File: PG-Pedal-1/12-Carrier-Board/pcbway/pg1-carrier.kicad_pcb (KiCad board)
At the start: 2 copper layers, 111 x 42.2 mm, 97 parts, among them J1 line in, J10 seed audio, J19 pg-hp, J2 line out, J20 pg-line, J3 no amp, J4 phones, J9 9V in, U1 LP2985-33, U4 NE5532, U5 NE5532, U6 NE5532, U7 TPA6139A2, U8 TPA6139A2, U9 TLV7031

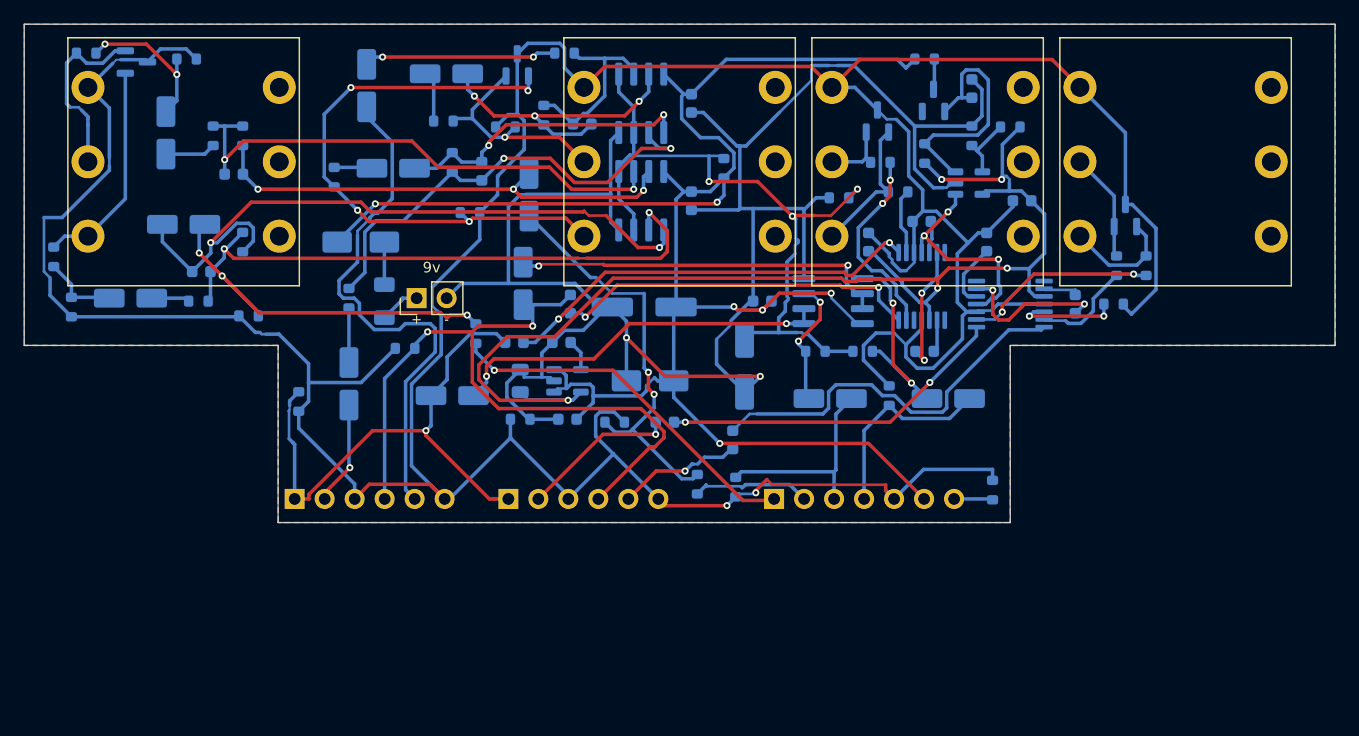
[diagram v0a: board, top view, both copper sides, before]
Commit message: Carrier board: JLCPCB files (basic parts where possible), ceramic caps instead of electrolytics
Co-Authored-By: Claude Opus 5.5 <noreply@anthropic.com>
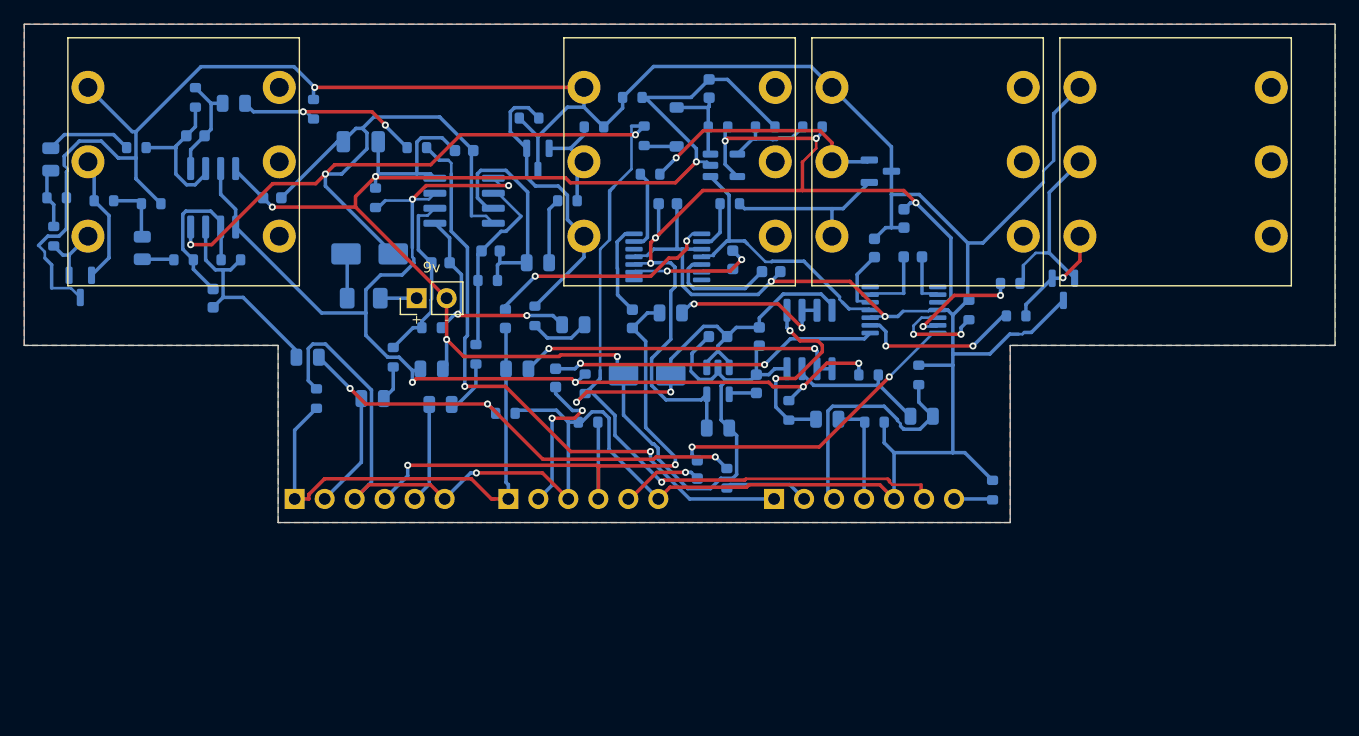
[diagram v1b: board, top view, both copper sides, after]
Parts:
- C1: value 47uF 25V -> 22uF 25V; footprint CP_Elec_6.3x5.8 -> C_1206_3216Metric
- C10, C12, C13, C14, C15, C17, C30, C32, C33, C34, C35, C37: footprint CP_Elec_4x5.4 -> C_0805_2012Metric
- C2: value 47uF 16V -> 22uF 25V; footprint CP_Elec_5x5.4 -> C_0805_2012Metric
- D50: value BAT54 -> 1N4148W; footprint SOT-23 -> D_SOD-123
- R18, R38: value 22k -> 51k
- R19, R39: value 43k -> 100k
- moved R2 39.2 mm to (74.2, 44.5), turned to 90 degrees
- moved U4 36.3 mm to (60.5, 44.5), turned to -90 degrees
- moved C66 35.5 mm to (65.5, 44.5), turned to 180 degrees
- moved R70 28.9 mm to (96.0, 36.0)
- moved C1 27.8 mm to (73.0, 39.8), turned to 0 degrees
- moved C35 27.7 mm to (79.8, 62.0), turned to 180 degrees
- moved R38 26.6 mm to (82.8, 57.8), turned to 90 degrees
- moved C2 26.5 mm to (79.0, 59.0), turned to 0 degrees
- moved R51 24.6 mm to (97.0, 39.2), turned to -90 degrees
- moved C32 23.3 mm to (68.5, 58.0), turned to 0 degrees
- moved C50 22.2 mm to (102.5, 35.2)
- moved D50 21.9 mm to (99.8, 38.5)
- moved R1 21.7 mm to (92.0, 60.2)
- moved U7 21.6 mm to (99.0, 49.5), turned to 180 degrees
- moved U9 20.8 mm to (103.8, 41.8)
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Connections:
- D50 pad 1: EN_RC -> +9V_SENSE
- D50 pad 2: (no net) -> EN_RC
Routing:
- net IN_O_L: track 57.7 -> 9.09 mm, vias 2 -> 0
- net IN_N_L: track 50.7 -> 12.6 mm, vias 2 -> 0
- net VREF: track 61.8 -> 99.3 mm, vias 3 -> 6
- net LINE_W_R: track 44.9 -> 8.51 mm
- net IN_N_R: track 45.1 -> 14.4 mm, vias 2 -> 0
- net +9V: track 154.8 -> 182.1 mm
- net JLO_L: track 50.2 -> 24.8 mm, vias 4 -> 0
- net LO_N_L: track 39.2 -> 15.1 mm, vias 2 -> 0
- net NA_IN_R: track 30.9 -> 7.99 mm, vias 2 -> 0
- net IN_O_R: track 41.1 -> 18.6 mm, vias 3 -> 0
- net +3V3A: track 104.8 -> 82.6 mm
- net SEED_IN_L: track 31.2 -> 52.7 mm, vias 1 -> 2
- net OB_O_R: track 32.3 -> 14.1 mm
- net SEED_IN_RAW_L: track 33.5 -> 16.4 mm, vias 3 -> 2
- net NA_IN_L: track 35.9 -> 19.9 mm
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
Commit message: Carrier board: all parts on one side, labels clear of pads, 0 DRC warnings
Co-Authored-By: Claude Opus 5.5 <noreply@anthropic.com>
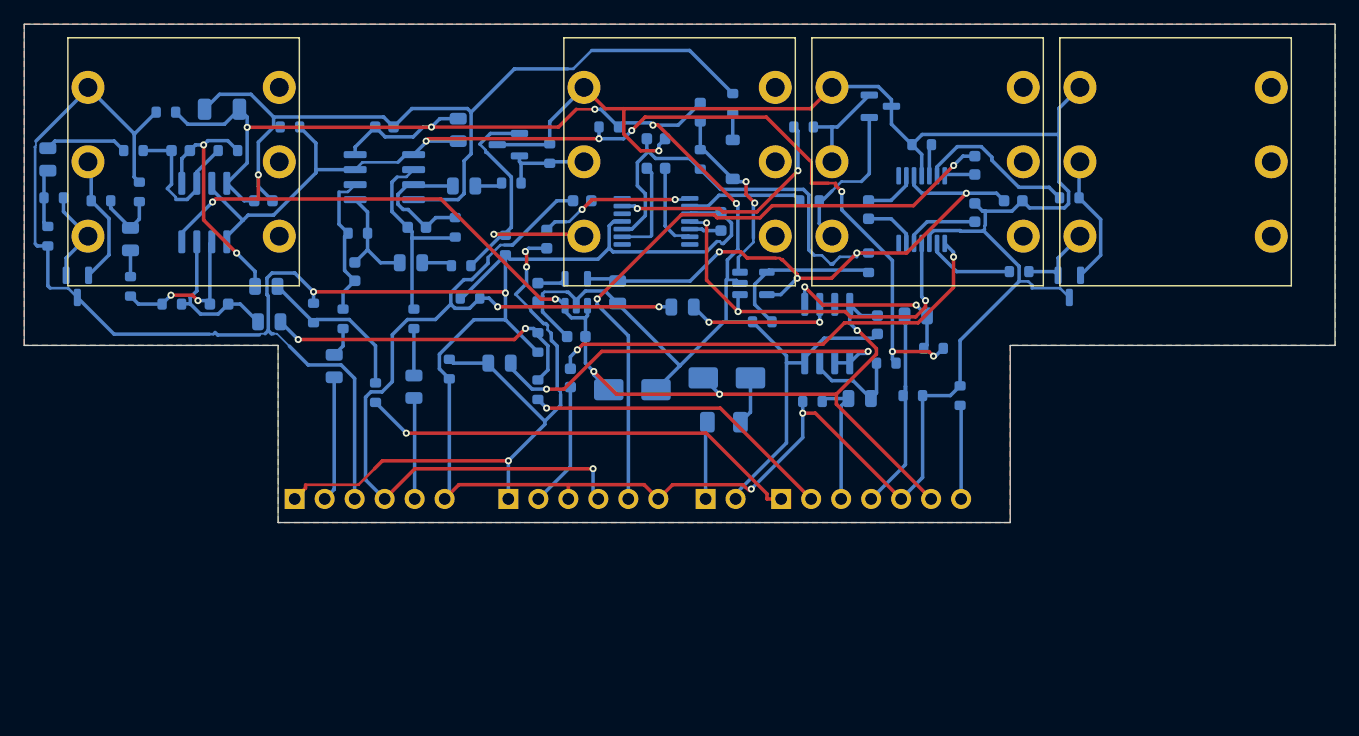
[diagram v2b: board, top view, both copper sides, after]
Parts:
- J9: footprint PinHeader_1x02_P2.54mm_Vertical -> PinHeader_1x02_P2.54mm_Horizontal; moved to B.Cu
- moved R70 39.5 mm to (56.5, 37.2)
- moved C39 34.9 mm to (125.0, 41.8), turned to -90 degrees
- moved R1 33.1 mm to (67.0, 38.5), turned to 0 degrees
- moved F1 32.3 mm to (103.8, 63.5), turned to 0 degrees
- moved D1 32.0 mm to (104.0, 59.8), turned to 0 degrees
- moved J9 29.8 mm to (102.2, 70.0), turned to -90 degrees
- moved R13 21.0 mm to (74.2, 61.0), turned to -90 degrees
- moved R2 20.6 mm to (94.0, 38.5), turned to 0 degrees
- moved C2 20.4 mm to (81.2, 38.8), turned to 90 degrees
- moved C3 20.1 mm to (88.0, 52.5), turned to -90 degrees
- moved R33 17.7 mm to (88.0, 60.8)
- moved R14 17.2 mm to (69.0, 54.2)
- moved R53 16.5 mm to (107.0, 55.0), turned to 180 degrees
- moved C12 15.7 mm to (65.0, 52.0)
- moved C17 14.7 mm to (77.2, 50.0)
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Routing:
- net HP_W_R: track 6.99 -> 55.2 mm, vias 1 -> 2
- net BUS_R: track 51.6 -> 77.9 mm, vias 2 -> 3
- net HP_IN_R: track 26.1 -> 2.60 mm, vias 2 -> 0
- net SEED_IN_R: track 7.17 -> 26.6 mm, vias 0 -> 1
- net SEED_IN_L: track 52.7 -> 38.0 mm, vias 2 -> 1
- net BUS_L: track 42.8 -> 56.8 mm, vias 0 -> 3
- net NA_O_R: track 6.88 -> 20.4 mm, vias 0 -> 2
- net JNA_R: track 21.4 -> 8.81 mm, vias 1 -> 0
- net IN_O_L: track 9.09 -> 21.6 mm, vias 0 -> 2
- net +9V: track 182.1 -> 170.0 mm
- net SEED_IN_RAW_R: track 39.7 -> 27.7 mm, vias 3 -> 2
- net HP_IN_L: track 28.0 -> 39.9 mm
- net LO_O_L: track 19.8 -> 9.38 mm, vias 2 -> 0
- net SEED_OUT_L: track 21.3 -> 11.1 mm
- net MUTE_N: track 23.6 -> 33.5 mm, vias 0 -> 3
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
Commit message: Carrier board: Neutrik NMJ6HCD2 jacks fitted by the assembler; jack holes 11.4 mm
Co-Authored-By: Claude Opus 5.5 <noreply@anthropic.com>
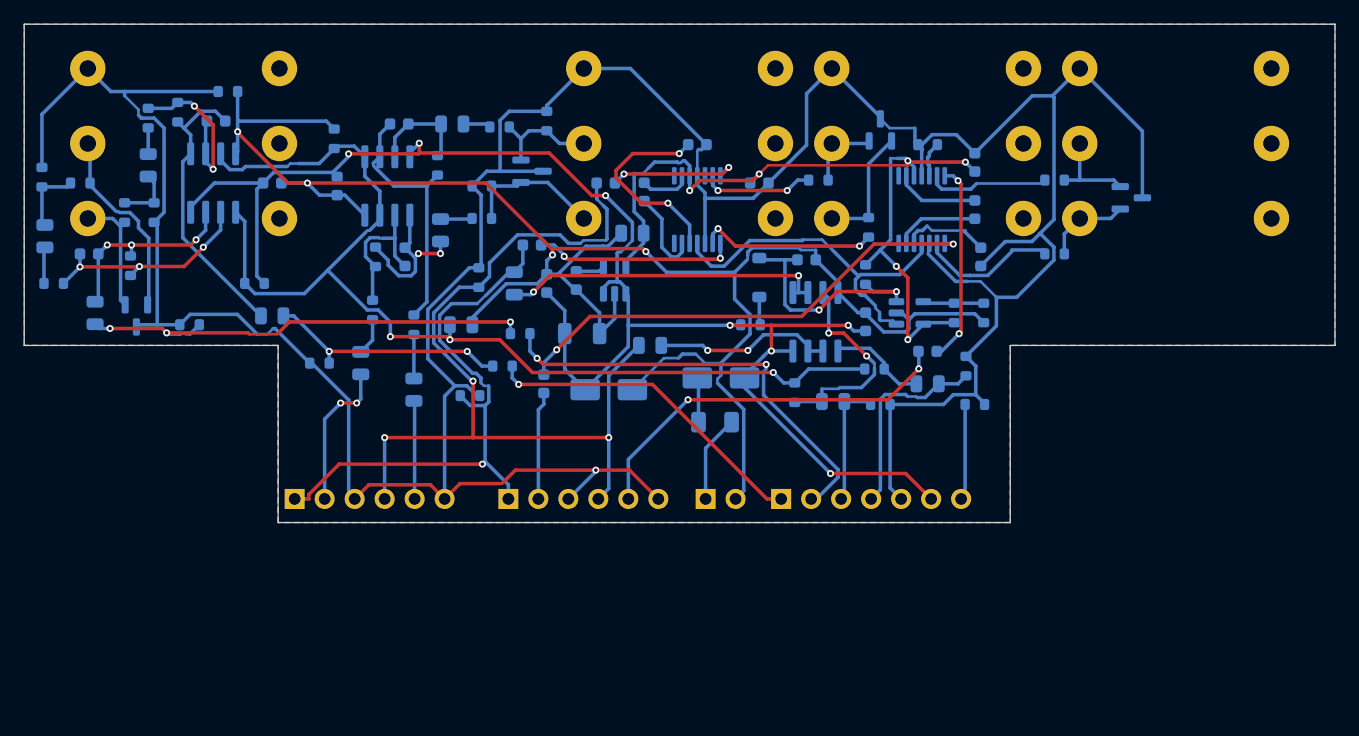
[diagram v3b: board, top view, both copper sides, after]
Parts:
- J1, J2, J3, J4: footprint Jack_6.35mm_TRS_PCB_A-1122 -> Jack_6.35mm_Neutrik_NMJ6HCD2_Horizontal
- moved C1 35.9 mm to (91.8, 56.0)
- moved R34 29.5 mm to (58.5, 55.2), turned to 180 degrees
- moved R2 23.3 mm to (70.8, 39.5), turned to 90 degrees
- moved R51 18.8 mm to (106.0, 55.2), turned to 0 degrees
- moved R53 18.8 mm to (125.8, 54.2), turned to -90 degrees
- moved J4 17.3 mm to (133.9, 46.2), turned to 90 degrees
- moved J1 17.3 mm to (49.9, 46.2), turned to 90 degrees
- moved J2 17.3 mm to (91.9, 46.2), turned to 90 degrees
- moved J3 17.3 mm to (112.9, 46.2), turned to 90 degrees
- moved R50 17.1 mm to (115.8, 51.0), turned to -90 degrees
- moved C2 16.5 mm to (81.5, 55.2), turned to 0 degrees
- moved C39 16.2 mm to (121.0, 57.5), turned to 0 degrees
- moved C50 15.4 mm to (110.8, 49.8), turned to 0 degrees
- moved C32 14.8 mm to (50.5, 54.2), turned to -90 degrees
- moved R1 13.6 mm to (64.0, 51.8), turned to 180 degrees
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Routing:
- net +9V: track 170.0 -> 131.6 mm, vias 6 -> 7
- net AGND: track 338.3 -> 306.3 mm, vias 5 -> 1
- net HP_W_R: track 55.2 -> 32.6 mm
- net +3V3A: track 85.0 -> 69.2 mm, vias 4 -> 6
- net NA_VSS: track 2.69 -> 17.1 mm, vias 0 -> 2
- net HP_IN_R: track 2.60 -> 16.9 mm, vias 0 -> 2
- net JLO_L: track 25.5 -> 11.9 mm, vias 1 -> 0
- net SEED_IN_RAW_R: track 27.7 -> 40.2 mm, vias 2 -> 3
- net NA_O_R: track 20.4 -> 9.48 mm
- net SEED_IN_R: track 26.6 -> 37.3 mm, vias 1 -> 2
- net GND: track 147.8 -> 158.2 mm, vias 5 -> 4
- net SEED_IN_L: track 38.0 -> 28.0 mm
- net EN_REF: track 14.0 -> 5.16 mm
- net OB_P_L: track 9.06 -> 17.9 mm, vias 0 -> 2
- net OB_O_L: track 36.1 -> 27.4 mm
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
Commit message: Carrier board: inputs left / outputs right with a diamond divider, (IN)/(OUT) labels, pg-1 artwork; face print IN/OUT tags
Co-Authored-By: Claude Opus 5.5 <noreply@anthropic.com>
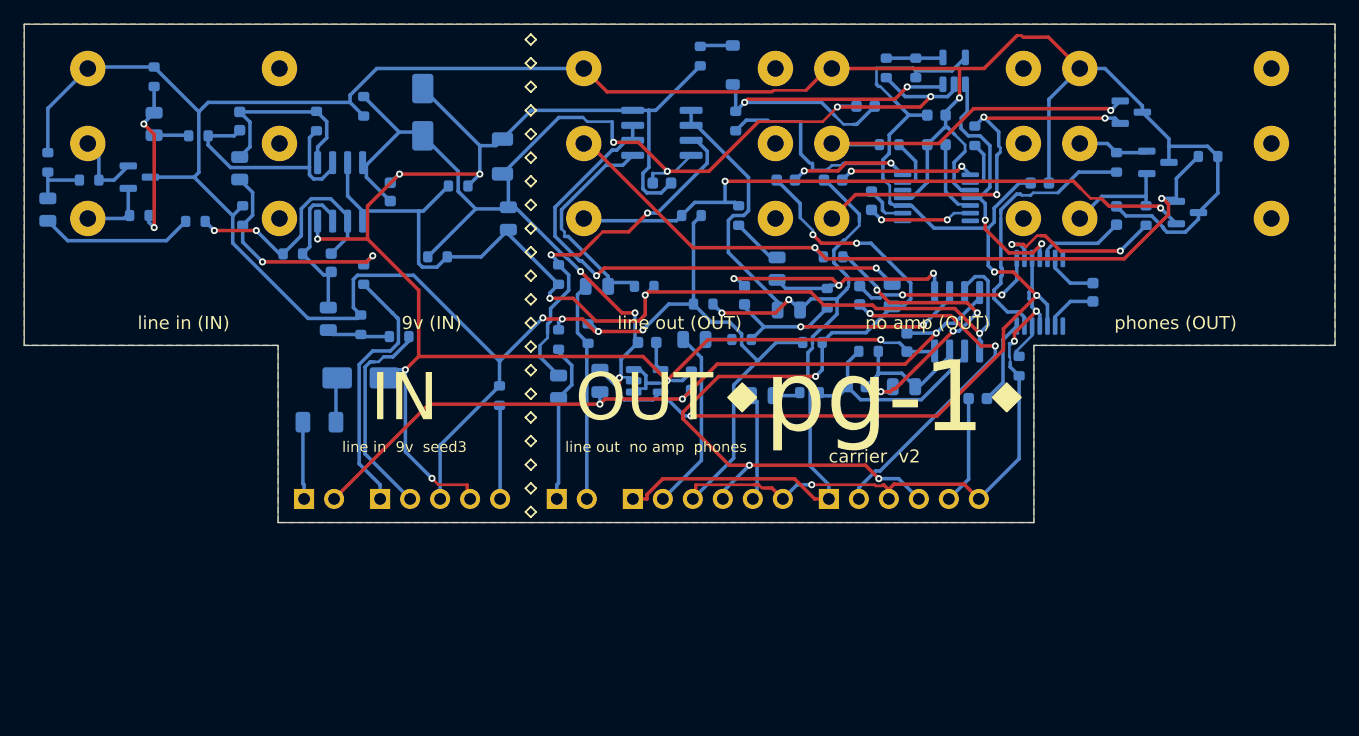
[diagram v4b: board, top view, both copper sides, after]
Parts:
- added J11: seed3 out, PinHeader_1x02_P2.54mm_Horizontal, B.Cu at (89.6, 70.0)
- J10: value seed audio -> seed3 in + power; footprint PinHeader_1x07_P2.54mm_Horizontal -> PinHeader_1x05_P2.54mm_Horizontal
- moved R41 56.1 mm to (144.8, 41.0), turned to 0 degrees
- moved D62 55.6 mm to (143.0, 45.8)
- moved C68 50.0 mm to (119.2, 56.8), turned to 90 degrees
- moved U6 49.6 mm to (123.5, 55.0), turned to -90 degrees
- moved C36 44.7 mm to (115.0, 60.5)
- moved C37 44.3 mm to (119.0, 60.5), turned to 180 degrees
- moved R71 40.3 mm to (84.8, 61.2), turned to 90 degrees
- moved R39 39.8 mm to (116.0, 57.5), turned to 0 degrees
- moved R19 38.4 mm to (112.5, 53.0)
- moved J9 34.0 mm to (68.2, 70.0)
- moved R38 34.0 mm to (111.0, 61.0), turned to 0 degrees
- moved J10 34.0 mm to (74.6, 70.0)
- moved F1 33.5 mm to (69.5, 63.5), turned to 0 degrees
- moved R36 32.1 mm to (92.2, 56.0)
- moved R18 31.3 mm to (105.2, 56.5), turned to 0 degrees
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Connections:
- J10 pad 3: SEED_OUT_L -> AGND
- J10 pad 4: SEED_OUT_R -> +9V
- J10 pad 5: AGND -> DGND
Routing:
- net JLO_R: track 9.25 -> 63.8 mm, vias 0 -> 2
- net JLO_L: track 11.9 -> 55.5 mm, vias 0 -> 2
- net +3V3A: track 69.2 -> 112.0 mm, vias 6 -> 3
- net SEED_IN_RAW_R: track 40.2 -> 5.40 mm, vias 3 -> 0
- net AGND: track 306.3 -> 336.9 mm, vias 1 -> 8
- net OB_O_R: track 15.2 -> 43.4 mm
- net JNA_L: track 10.4 -> 34.9 mm, vias 0 -> 3
- net HP_IN_L: track 40.6 -> 16.2 mm
- net GND: track 158.2 -> 181.9 mm, vias 4 -> 10
- net JNA_R: track 6.48 -> 30.1 mm, vias 0 -> 1
- net HP_W_R: track 32.6 -> 9.19 mm, vias 2 -> 0
- net LO_C_R: track 2.33 -> 25.6 mm, vias 0 -> 4
- net HP_W_L: track 9.17 -> 30.9 mm, vias 0 -> 2
- net SEED_IN_R: track 37.3 -> 17.7 mm, vias 2 -> 0
- net +9V: track 131.6 -> 146.5 mm
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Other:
- outline, holes or cut-outs redrawn
- board text added: "9v (IN)"
- board text added: "IN"
- board text added: "OUT"
- board text added: "carrier v2"
- board text added: "line in (IN)"
- board text added: "line in 9v seed3"
- board text added: "line out (OUT)"
- board text added: "line out no amp phones"
- board text added: "no amp (OUT)"
- board text added: "pg-1"
- board text added: "phones (OUT)"
- board text added: "seed3 (IN)"
- board text added: "seed3 (OUT)"
- board text removed: "line in"
- board text removed: "line out"
- board text removed: "no amp"
- board text removed: "pg-1 carrier v2"
- board text removed: "phones"
- board text removed: "seed3"
